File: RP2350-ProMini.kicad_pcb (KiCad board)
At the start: 4 copper layers, 17.8 x 41.9 mm, 44 parts, among them J1 CONN_L, J2 CONN_U, J3 CONN_R2, J4 CONN_R, J5 CONN_R3, J6 USB_B_Micro, J7 CONN_JTAG, Q1 AO3400A, U1 W25Q128JVS, U2 RP2350A-QFN60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

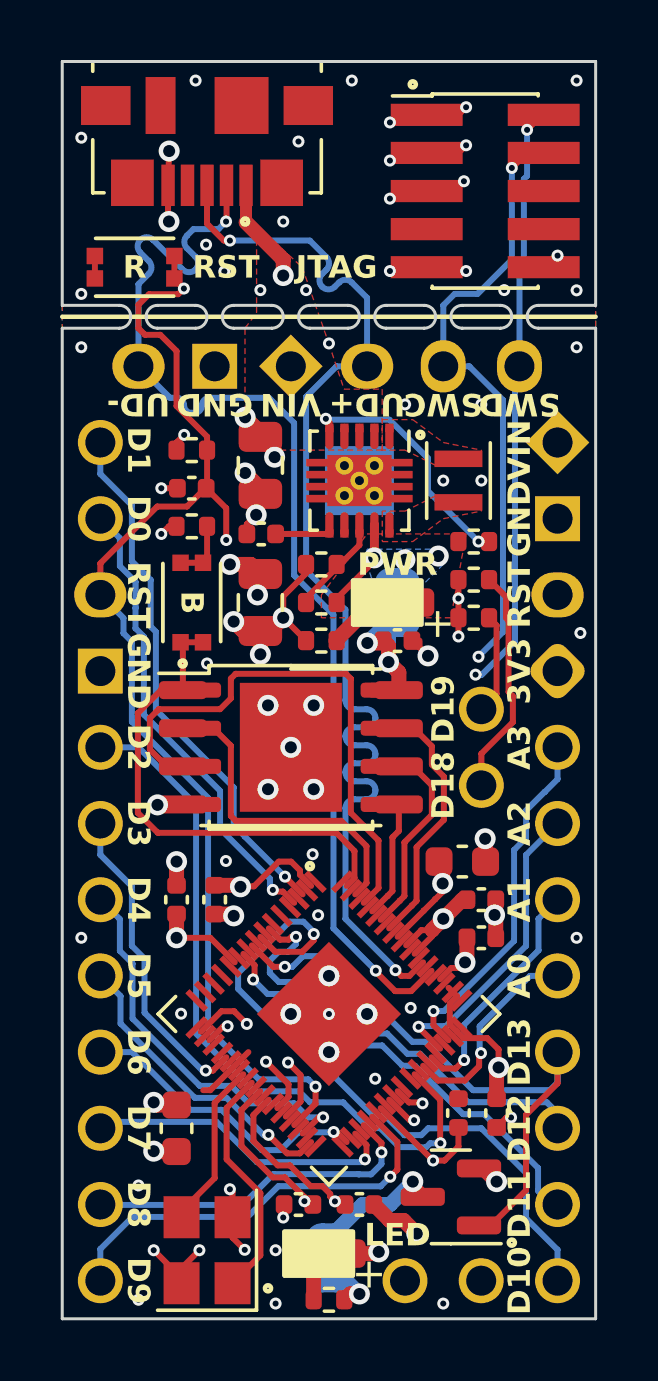
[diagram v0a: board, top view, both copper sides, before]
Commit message: Added some routing
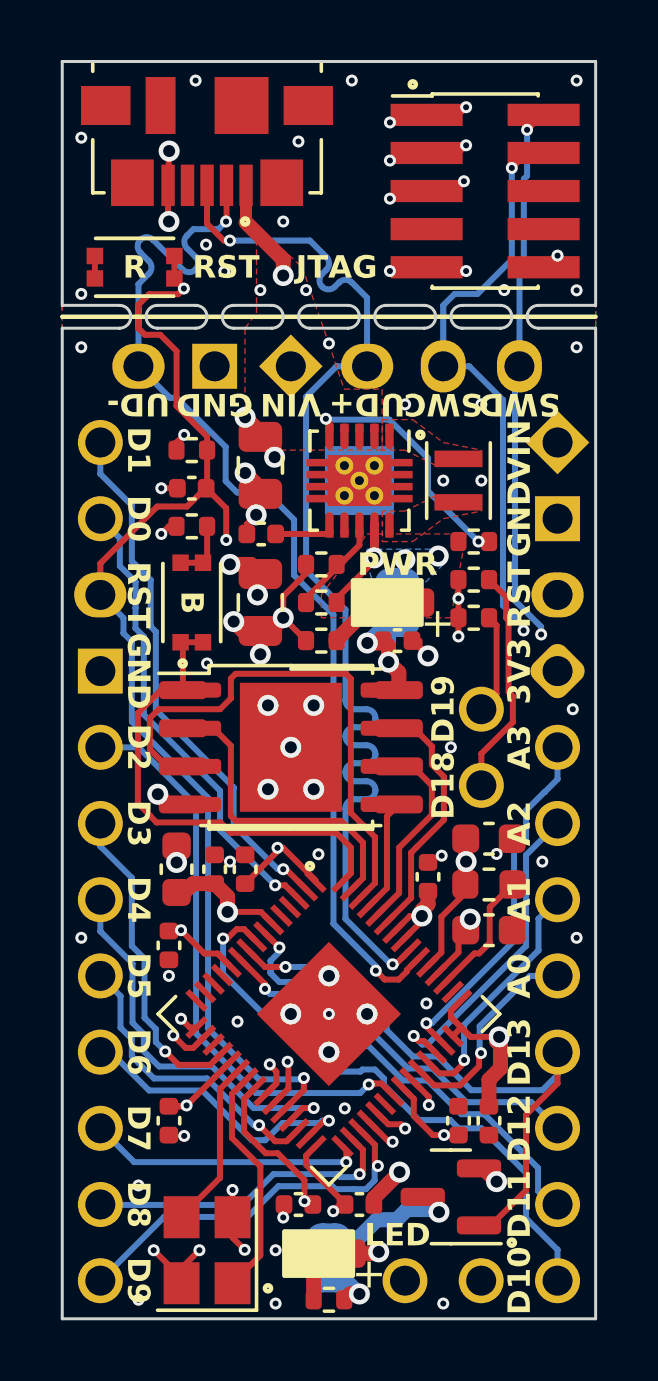
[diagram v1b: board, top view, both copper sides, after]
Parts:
- added C16: 2.2uF, Capacitor_SMD:C_0603_1608Metric, F.Cu at (148.8, 111.0)
- added C17: 100nF, Capacitor_SMD:C_0402_1005Metric, F.Cu at (140.7, 112.0)
- added L2: 3.3uH, Inductor_SMD:L_0603_1608Metric, F.Cu at (148.8, 112.5)
- moved C1 12.3 mm to (148.8, 114.0), turned to 0 degrees
- moved C5 9.53 mm to (138.4, 112.0), turned to 90 degrees
- moved C9 9.18 mm to (139.7, 112.0), turned to 90 degrees
- moved C10 7.52 mm to (138.2, 120.4)
- moved C7 2.03 mm to (142.5, 123.2), turned to 180 degrees
- moved C8 2.03 mm to (144.5, 123.2), turned to 0 degrees
- moved C4 1.93 mm to (146.8, 112.3), turned to 90 degrees
- moved C3 1.55 mm to (138.2, 114.6), turned to -90 degrees
- moved C6 0.36 mm to (148.8, 120.4)
- moved C11 0.25 mm to (147.8, 120.4)
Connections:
- U2 pad 46: unconnected-(U2-VREG_AVDD-Pad46) -> +3V3
- U2 pad 47: unconnected-(U2-VREG_PGND-Pad47) -> GND
- U2 pad 48: unconnected-(U2-VREG_LX-Pad48) -> VERG_LX
- U2 pad 49: unconnected-(U2-VREG_VIN-Pad49) -> +3V3
- U2 pad 50: unconnected-(U2-VREG_FB-Pad50) -> +1V1
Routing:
- net +1V1: track 23.4 -> 38.8 mm, vias 3 -> 4
- net GND: track 35.6 -> 30.3 mm
- net D2: track 24.0 -> 19.3 mm
- net VERG_LX: track 0.00 -> 4.34 mm
- net D10_SS: track 22.7 -> 19.6 mm
- net USB_DN: track 39.2 -> 36.9 mm
- net XIN: track 7.65 -> 5.70 mm
- net D18_SDA: track 23.4 -> 21.5 mm
- net D9: track 14.2 -> 12.6 mm
- net D12_MISO: track 15.1 -> 13.6 mm
- net SWD: track 40.5 -> 39.0 mm
- net SWCLK: track 41.8 -> 40.5 mm
- net D7: track 10.5 -> 9.24 mm
- net D20: track 8.90 -> 7.60 mm
- net D19_SCL: track 20.0 -> 21.0 mm
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- removed copper zone on In1.Cu, net GND

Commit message: Moved staff around.
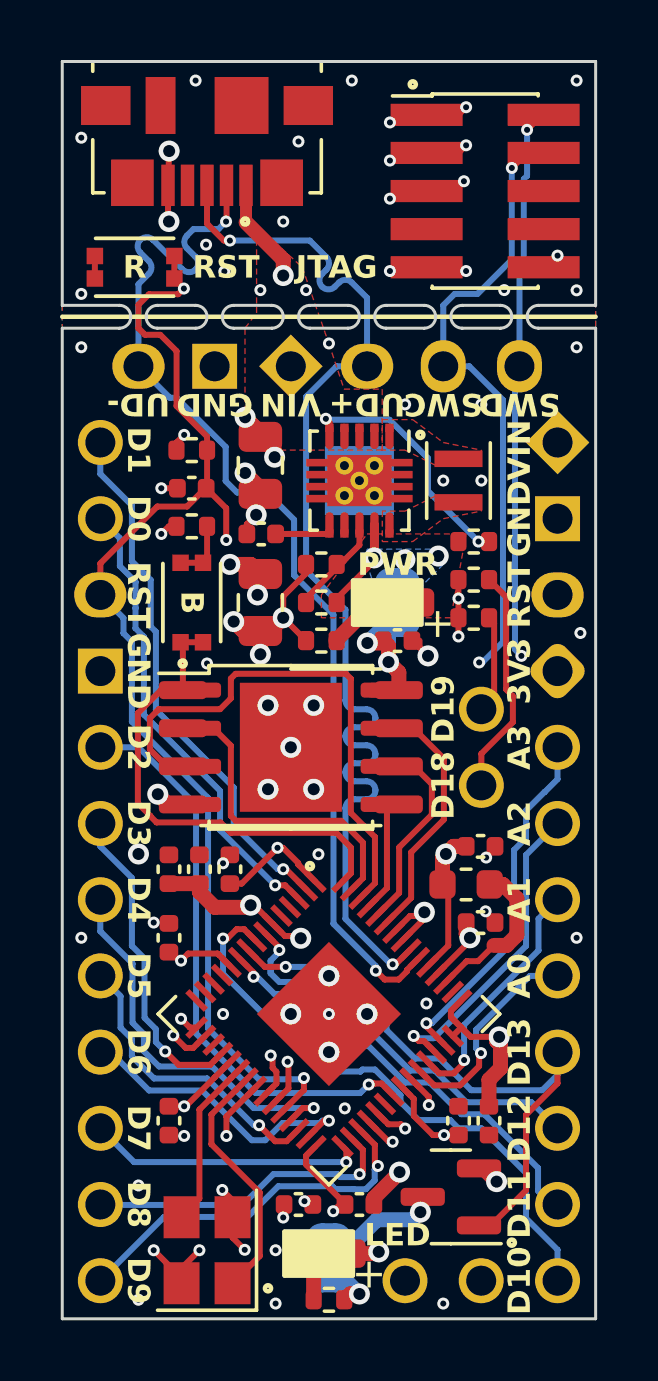
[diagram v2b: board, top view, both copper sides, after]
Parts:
- removed C17: 100nF, Capacitor_SMD:C_0402_1005Metric
- C1, C16, C5: footprint Capacitor_SMD:C_0603_1608Metric -> Capacitor_SMD:C_0402_1005Metric
- moved C4 6.61 mm to (140.2, 112.0)
- moved L2 0.76 mm to (148.1, 112.5)
- moved C9 0.51 mm to (139.2, 112.0)
- moved C1 0.38 mm to (148.6, 113.8)
- moved C16 0.38 mm to (148.6, 111.3)
- moved C5 0.25 mm to (138.2, 112.0)
- moved C3 0.25 mm to (138.2, 114.3), turned to 90 degrees
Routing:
- net +1V1: track 38.8 -> 23.7 mm, vias 4 -> 6
- net VERG_LX: track 4.34 -> 5.41 mm
- net SWCLK: track 40.5 -> 41.3 mm
- net D20: track 7.60 -> 6.96 mm
- net QSPI_SCLK: track 6.47 -> 7.02 mm
- net XOUT: track 7.82 -> 8.37 mm
- net GND: track 30.3 -> 30.4 mm, vias 73 -> 71
- added copper zone on In1.Cu, net +1V1

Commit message: Moved staff around.
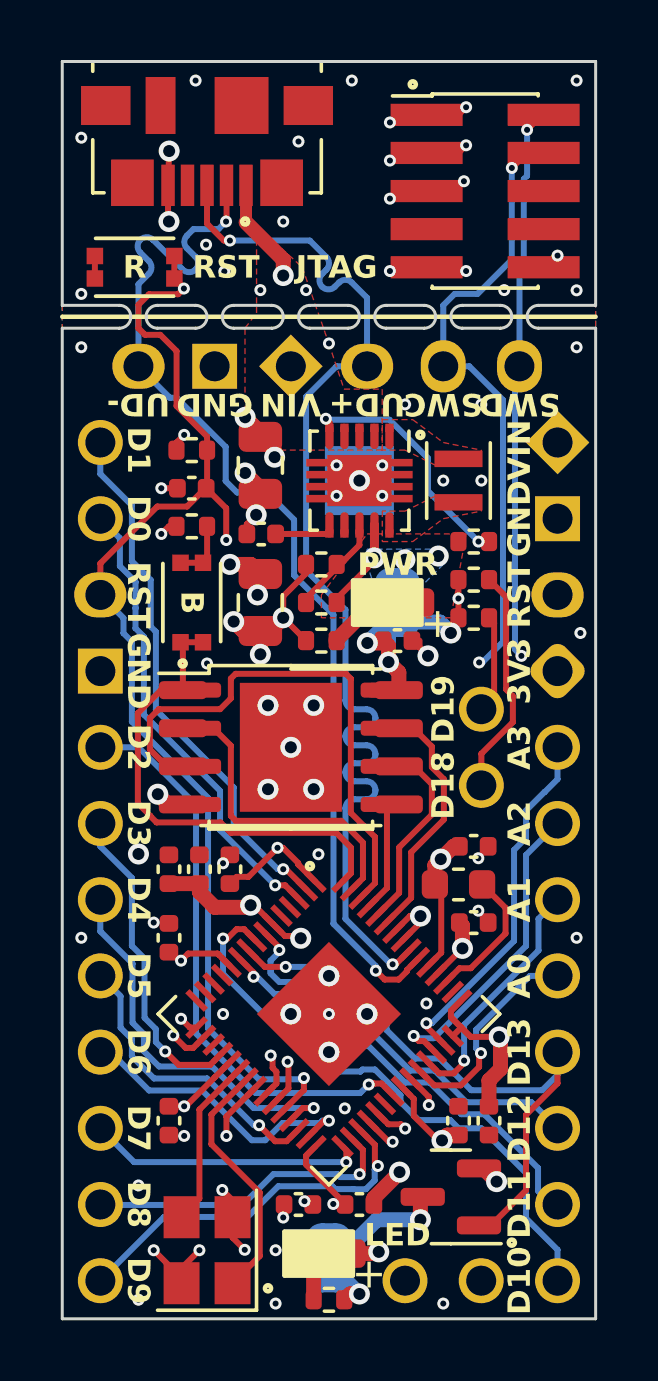
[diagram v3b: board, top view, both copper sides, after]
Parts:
- moved L2 0.25 mm to (147.8, 112.5)
- moved C1 0.23 mm to (148.3, 113.8)
- moved C16 0.23 mm to (148.3, 111.3)
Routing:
- net +3V3: track 39.5 -> 54.6 mm
- net VERG_LX: track 5.41 -> 4.69 mm
- net GND: vias 71 -> 76

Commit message: Improved USB data lines
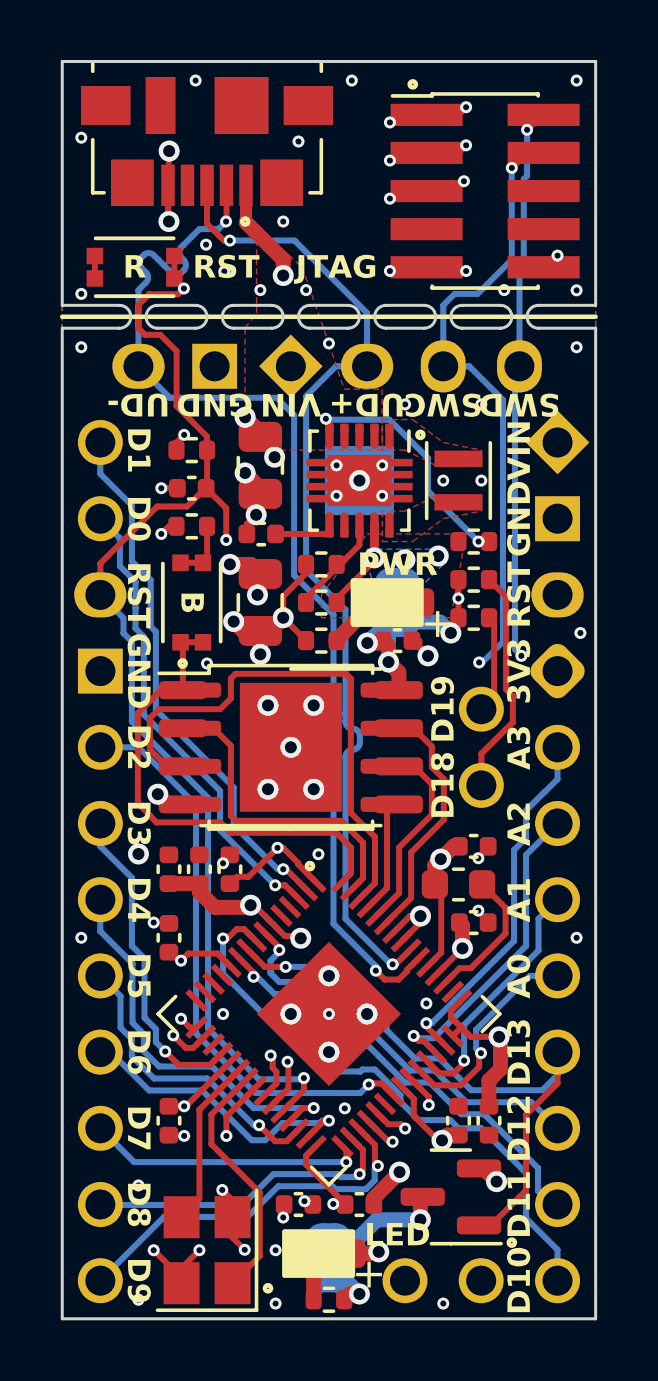
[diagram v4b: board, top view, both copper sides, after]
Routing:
- net USB_DP: track 38.7 -> 33.5 mm

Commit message: Moved staff around.
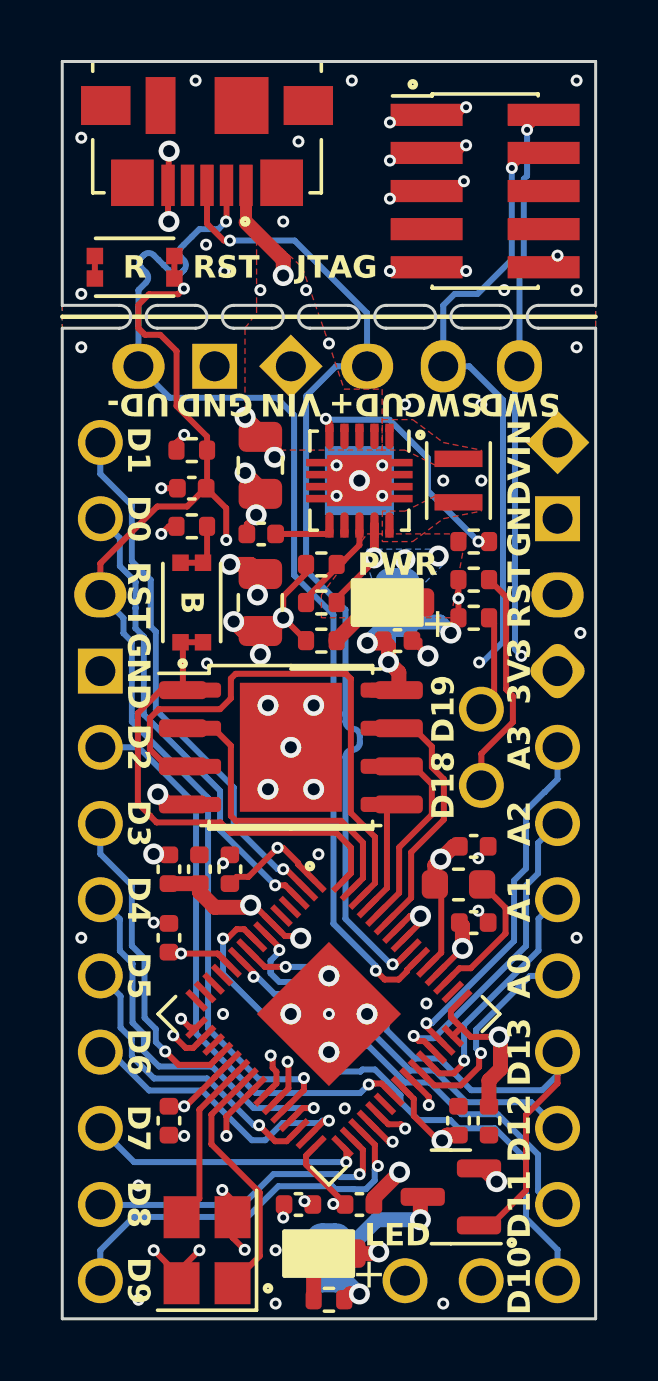
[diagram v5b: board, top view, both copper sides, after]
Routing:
- net D9: track 12.6 -> 13.2 mm

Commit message: Moved staff around.
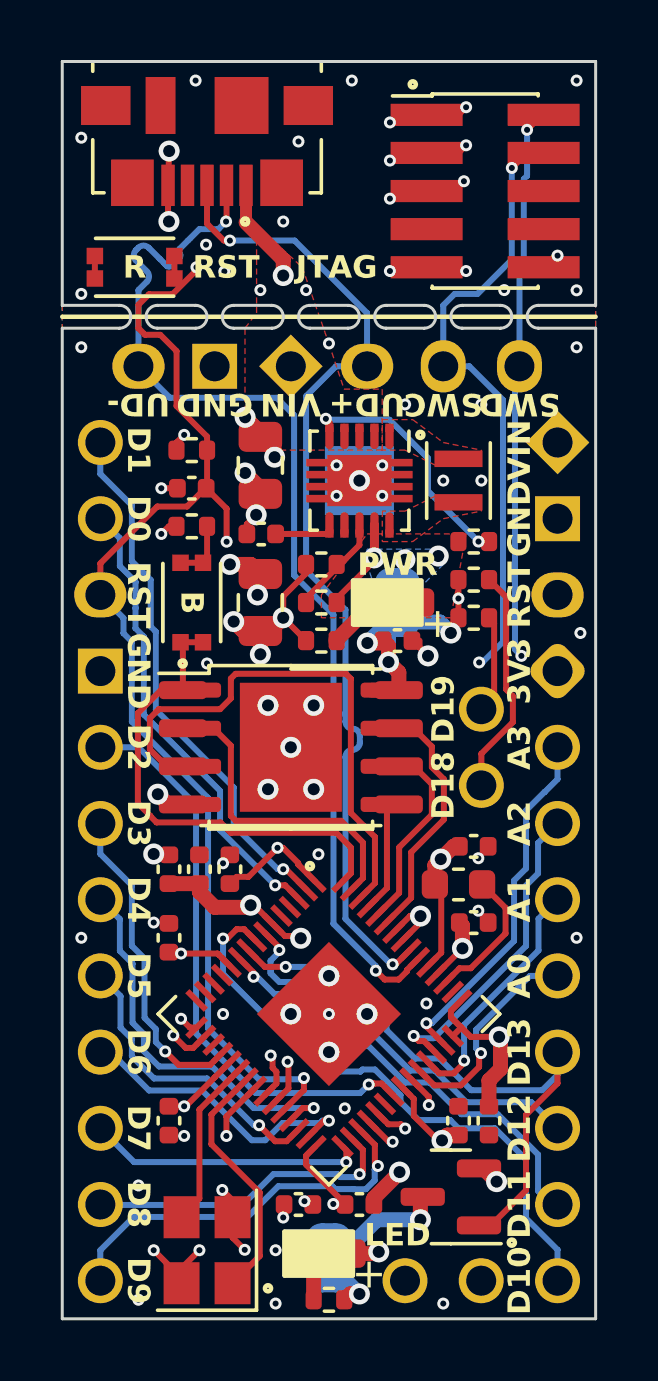
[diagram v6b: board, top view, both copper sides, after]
